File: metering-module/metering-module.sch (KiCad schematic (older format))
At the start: 36 parts, among them J1 North, J2 South, J3 West, J4 East, Q1 MMBT3904, Q2 MMBT3904, U1 LTV-817S, U2 LTV-817S, U3 BA033CC0FP-E2, U4 MAX3486, U5 MAX3486, U6 MCP23008-xSO

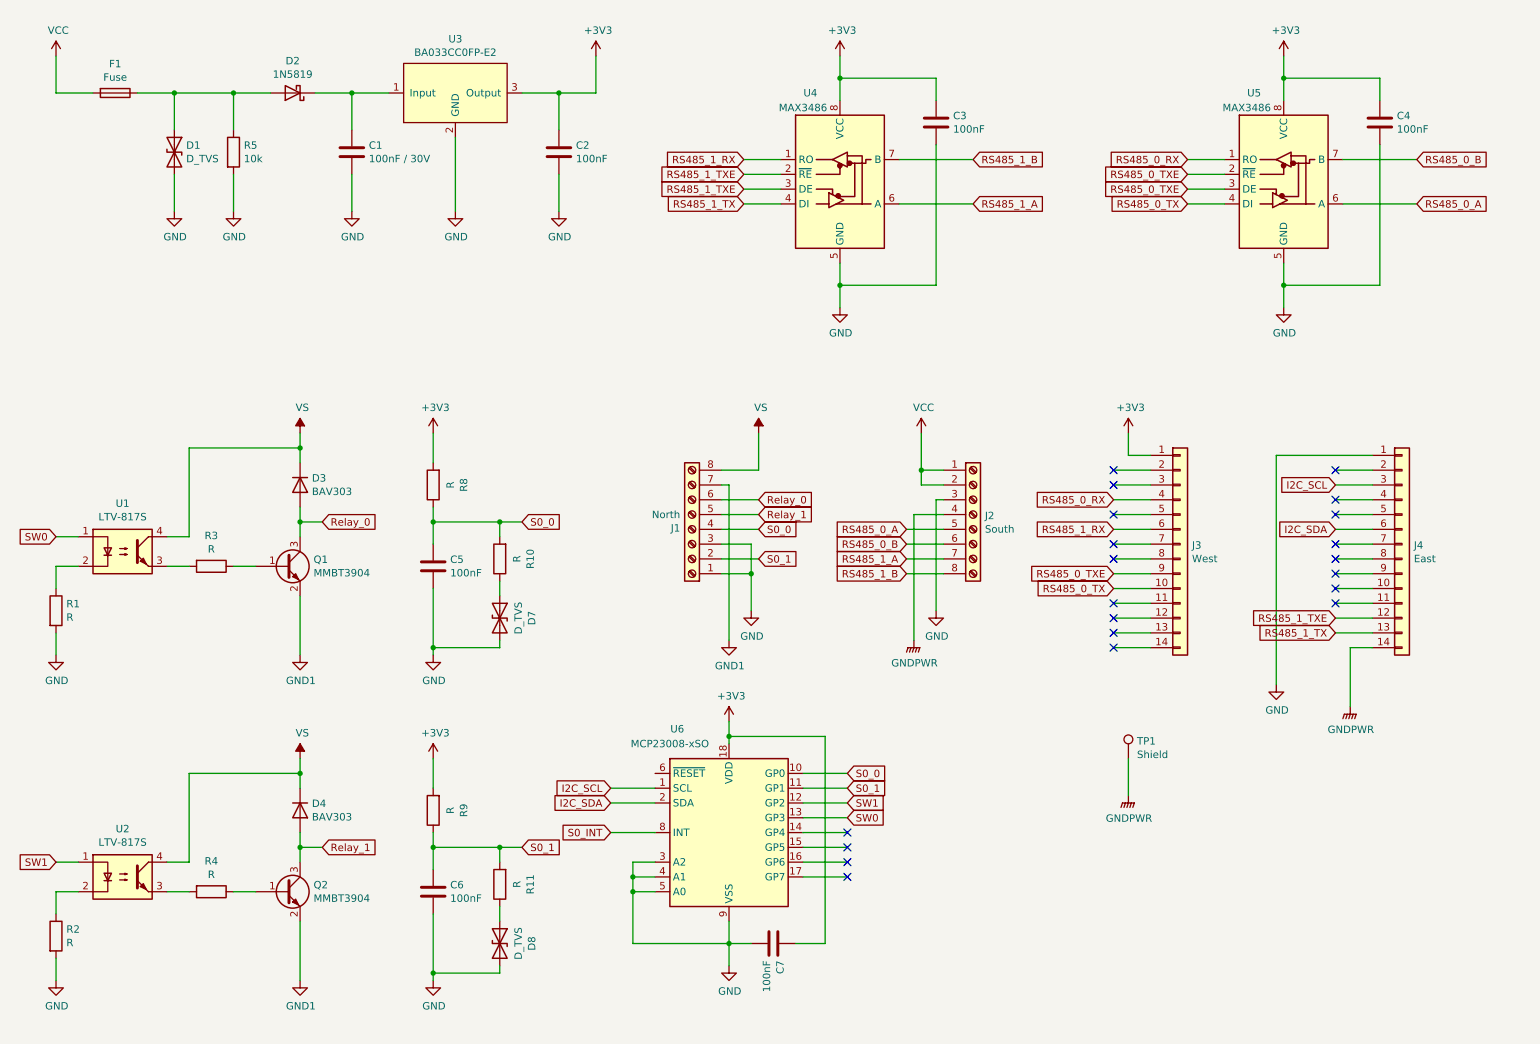
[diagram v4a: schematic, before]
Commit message: Introduce new serial numbering scheme
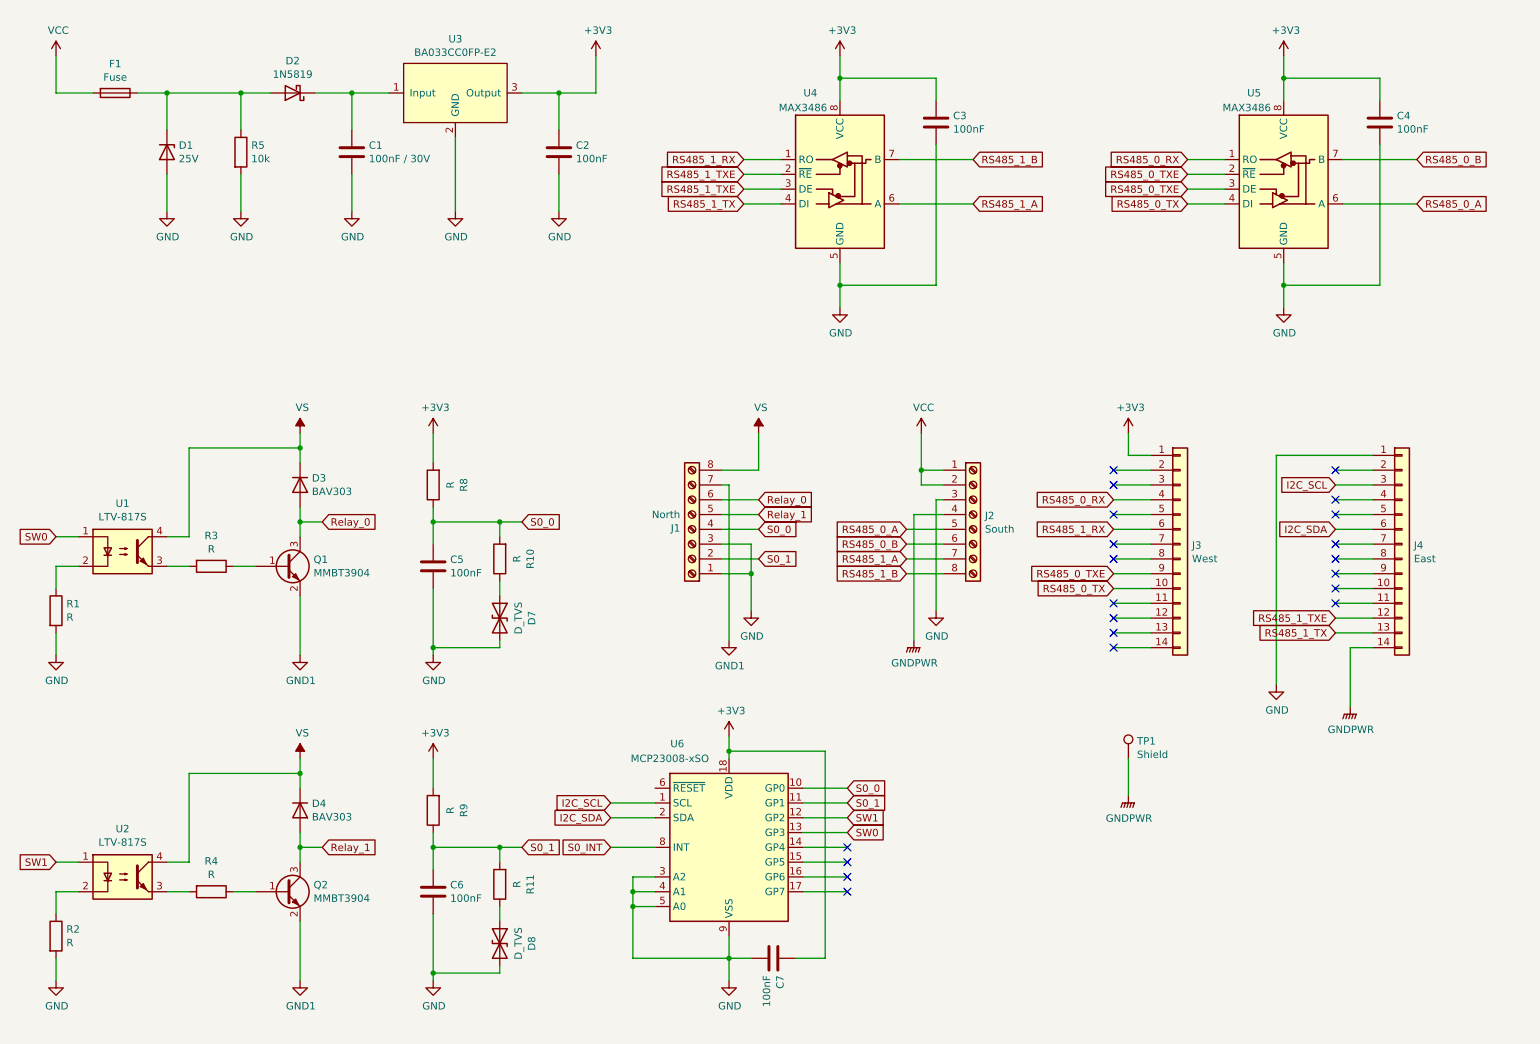
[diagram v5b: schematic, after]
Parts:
- removed D1: D_TVS, Diode_SMD:D_SOD-323_HandSoldering, symbol Device:D_TVS
- added D1: 25V, Diode_SMD:D_SOD-523, symbol Device:D_Zener
- C1: Price (none) -> 0.24; Product (none) -> https://www.mouser.de/ProductDetail/KEMET/C1206C104M6RACTU?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
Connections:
- net GND: now also D1.2 (A)
- net at D2.2 (A), F1.1, R5.1: now also D1.1 (K)
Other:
- moved on the sheet: C7, R5, U6
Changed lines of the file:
@@
-$EndComp
-$Comp
-L Device:D_TVS D1
-U 1 1 61930B40
-P 1950 1750
-F 0 "D1" V 1904 1830 50  0000 L CNN
-F 1 "D_TVS" V 1995 1830 50  0000 L CNN
-F 2 "Diode_SMD:D_SOD-323_HandSoldering" H 1950 1750 50  0001 C CNN
-F 3 "~" H 1950 1750 50  0001 C CNN
-	1    1950 1750
-	0    1    1    0
 $EndComp
 $Comp
@@
 L Device:R R5
 U 1 1 61931725
-P 2350 1750
-F 0 "R5" H 2420 1796 50  0000 L CNN
-F 1 "10k" H 2420 1705 50  0000 L CNN
-F 2 "Resistor_SMD:R_1206_3216Metric_Pad1.30x1.75mm_HandSolder" V 2280 1750 50  0001 C CNN
-F 3 "~" H 2350 1750 50  0001 C CNN
-	1    2350 1750
+P 2400 1750
+F 0 "R5" H 2470 1796 50  0000 L CNN
+F 1 "10k" H 2470 1705 50  0000 L CNN
+F 2 "Resistor_SMD:R_1206_3216Metric_Pad1.30x1.75mm_HandSolder" V 2330 1750 50  0001 C CNN
+F 3 "~" H 2400 1750 50  0001 C CNN
+	1    2400 1750
 	1    0    0    -1
 $EndComp
@@
 F 1 "100nF / 30V" H 3265 1705 50  0000 L CNN
 F 2 "Capacitor_SMD:C_1206_3216Metric_Pad1.33x1.80mm_HandSolder" H 3188 1600 50  0001 C CNN
-F 3 "~" H 3150 1750 50  0001 C CNN
+F 3 "https://www.mouser.de/datasheet/2/212/KEM_C1002_X7R_SMD-1102033.pdf" H 3150 1750 50  0001 C CNN
+F 4 "https://www.mouser.de/ProductDetail/KEMET/C1206C104M6RACTU?qs=F5EMLAvA7IBTviv6fCZN3A%3D%3D" H 3150 1750 50  0001 C CNN "Product"
+F 5 "0.24" H 3150 1750 50  0001 C CNN "Price"
 	1    3150 1750
 	1    0    0    -1
@@
 	3150 1350 3400 1350
 Wire Wire Line
-	2350 1600 2350 1350
-Wire Wire Line
-	1700 1350 1950 1350
-Connection ~ 2350 1350
-Wire Wire Line
-	2350 1350 2600 1350
-Wire Wire Line
-	1950 1600 1950 1350
-Connection ~ 1950 1350
-Wire Wire Line
-	1950 1350 2350 1350
+	2400 1600 2400 1350
+Wire Wire Line
+	1700 1350 1900 1350
+Wire Wire Line
+	1900 1600 1900 1350
 Wire Wire Line
 	4300 1350 4550 1350
@@
 L power:GND #PWR0106
 U 1 1 6193D7EC
-P 2350 2150
-F 0 "#PWR0106" H 2350 1900 50  0001 C CNN
-F 1 "GND" H 2355 1977 50  0000 C CNN
-F 2 "" H 2350 2150 50  0001 C CNN
-F 3 "" H 2350 2150 50  0001 C CNN
-	1    2350 2150
+P 2400 2150
+F 0 "#PWR0106" H 2400 1900 50  0001 C CNN
+F 1 "GND" H 2405 1977 50  0000 C CNN
+F 2 "" H 2400 2150 50  0001 C CNN
+F 3 "" H 2400 2150 50  0001 C CNN
+	1    2400 2150
 	1    0    0    -1
 $EndComp
@@
 L power:GND #PWR0107
 U 1 1 6193DD3C
-P 1950 2150
-F 0 "#PWR0107" H 1950 1900 50  0001 C CNN
-F 1 "GND" H 1955 1977 50  0000 C CNN
-F 2 "" H 1950 2150 50  0001 C CNN
-F 3 "" H 1950 2150 50  0001 C CNN
-	1    1950 2150
-	1    0    0    -1
-$EndComp
-Wire Wire Line
-	1950 1900 1950 2150
-Wire Wire Line
-	2350 2150 2350 1900
+P 1900 2150
+F 0 "#PWR0107" H 1900 1900 50  0001 C CNN
+F 1 "GND" H 1905 1977 50  0000 C CNN
+F 2 "" H 1900 2150 50  0001 C CNN
+F 3 "" H 1900 2150 50  0001 C CNN
+	1    1900 2150
+	1    0    0    -1
+$EndComp
+Wire Wire Line
+	1900 1900 1900 2150
+Wire Wire Line
+	2400 2150 2400 1900
 Wire Wire Line
 	3150 1900 3150 2150
@@
 Wire Wire Line
 	7000 3650 7000 3900
-Text GLabel 6500 5950 2    50   Input ~ 0
+Text GLabel 6500 6050 2    50   Input ~ 0
 S0_0
-Text GLabel 6500 6050 2    50   Input ~ 0
+Text GLabel 6500 6150 2    50   Input ~ 0
 S0_1
+Text GLabel 6500 6350 2    50   Input ~ 0
+SW0
 Text GLabel 6500 6250 2    50   Input ~ 0
-SW0
-Text GLabel 6500 6150 2    50   Input ~ 0
 SW1
 Wire Wire Line
@@
 L Interface_Expansion:MCP23008-xSO U6
 U 1 1 61EB4389
-P 5700 6350
-F 0 "U6" H 5350 7050 50  0000 C CNN
-F 1 "MCP23008-xSO" H 5300 6950 50  0000 C CNN
-F 2 "Package_SO:SOIC-18W_7.5x11.6mm_P1.27mm" H 5700 5300 50  0001 C CNN
-F 3 "http://ww1.microchip.com/downloads/en/DeviceDoc/MCP23008-MCP23S08-Data-Sheet-20001919F.pdf" H 7000 5150 50  0001 C CNN
-	1    5700 6350
+P 5700 6450
+F 0 "U6" H 5350 7150 50  0000 C CNN
+F 1 "MCP23008-xSO" H 5300 7050 50  0000 C CNN
+F 2 "Package_SO:SOIC-18W_7.5x11.6mm_P1.27mm" H 5700 5400 50  0001 C CNN
+F 3 "http://ww1.microchip.com/downloads/en/DeviceDoc/MCP23008-MCP23S08-Data-Sheet-20001919F.pdf" H 7000 5250 50  0001 C CNN
+	1    5700 6450
 	1    0    0    -1
 $EndComp
@@
 L Device:C C7
 U 1 1 61F32AD8
-P 6000 7100
-F 0 "C7" H 6115 7146 50  0000 L CNN
-F 1 "100nF" H 6115 7055 50  0000 L CNN
-F 2 "Capacitor_SMD:C_1206_3216Metric_Pad1.33x1.80mm_HandSolder" H 6038 6950 50  0001 C CNN
-F 3 "~" H 6000 7100 50  0001 C CNN
-	1    6000 7100
+P 6000 7200
+F 0 "C7" H 6115 7246 50  0000 L CNN
+F 1 "100nF" H 6115 7155 50  0000 L CNN
+F 2 "Capacitor_SMD:C_1206_3216Metric_Pad1.33x1.80mm_HandSolder" H 6038 7050 50  0001 C CNN
+F 3 "~" H 6000 7200 50  0001 C CNN
+	1    6000 7200
 	0    1    1    0
 $EndComp
@@
 L power:+3V3 #PWR0127
 U 1 1 61F36D22
-P 5700 5600
-F 0 "#PWR0127" H 5700 5450 50  0001 C CNN
-F 1 "+3V3" H 5715 5773 50  0000 C CNN
-F 2 "" H 5700 5600 50  0001 C CNN
-F 3 "" H 5700 5600 50  0001 C CNN
-	1    5700 5600
+P 5700 5700
+F 0 "#PWR0127" H 5700 5550 50  0001 C CNN
+F 1 "+3V3" H 5715 5873 50  0000 C CNN
+F 2 "" H 5700 5700 50  0001 C CNN
+F 3 "" H 5700 5700 50  0001 C CNN
+	1    5700 5700
 	1    0    0    -1
 $EndComp
@@
 L power:GND #PWR0133
 U 1 1 61F37FD9
-P 5700 7250
-F 0 "#PWR0133" H 5700 7000 50  0001 C CNN
-F 1 "GND" H 5705 7077 50  0000 C CNN
-F 2 "" H 5700 7250 50  0001 C CNN
-F 3 "" H 5700 7250 50  0001 C CNN
-	1    5700 7250
-	1    0    0    -1
-$EndComp
-Wire Wire Line
-	5700 5600 5700 5700
-Wire Wire Line
-	5700 6950 5700 7100
-Wire Wire Line
-	5850 7100 5700 7100
-Connection ~ 5700 7100
-Wire Wire Line
-	5700 7100 5700 7250
-Wire Wire Line
-	6150 7100 6350 7100
-Wire Wire Line
-	6350 7100 6350 5700
-Wire Wire Line
-	6350 5700 5700 5700
-Connection ~ 5700 5700
-Wire Wire Line
-	5700 5700 5700 5750
+P 5700 7350
+F 0 "#PWR0133" H 5700 7100 50  0001 C CNN
+F 1 "GND" H 5705 7177 50  0000 C CNN
+F 2 "" H 5700 7350 50  0001 C CNN
+F 3 "" H 5700 7350 50  0001 C CNN
+	1    5700 7350
+	1    0    0    -1
+$EndComp
+Wire Wire Line
+	5700 5700 5700 5800
+Wire Wire Line
+	5700 7050 5700 7200
+Wire Wire Line
+	5850 7200 5700 7200
+Connection ~ 5700 7200
+Wire Wire Line
+	5700 7200 5700 7350
+Wire Wire Line
+	6150 7200 6350 7200
+Wire Wire Line
+	6350 7200 6350 5800
+Wire Wire Line
+	6350 5800 5700 5800
+Connection ~ 5700 5800
+Wire Wire Line
+	5700 5800 5700 5850
 NoConn ~ 9800 4700
 NoConn ~ 8300 4900
@@
 NoConn ~ 8300 4200
 Wire Wire Line
-	6200 5950 6500 5950
-Wire Wire Line
 	6200 6050 6500 6050
 Wire Wire Line
-	6500 6150 6200 6150
-Wire Wire Line
-	6200 6250 6500 6250
-NoConn ~ 6500 6350
+	6200 6150 6500 6150
+Wire Wire Line
+	6500 6250 6200 6250
+Wire Wire Line
+	6200 6350 6500 6350
 NoConn ~ 6500 6450
 NoConn ~ 6500 6550
 NoConn ~ 6500 6650
-Wire Wire Line
-	6500 6350 6200 6350
+NoConn ~ 6500 6750
 Wire Wire Line
 	6500 6450 6200 6450
@@
 Wire Wire Line
 	6500 6650 6200 6650
+Wire Wire Line
+	6500 6750 6200 6750
+Text GLabel 4900 6250 0    50   Input ~ 0
+I2C_SDA
 Text GLabel 4900 6150 0    50   Input ~ 0
-I2C_SDA
-Text GLabel 4900 6050 0    50   Input ~ 0
 I2C_SCL
 Text GLabel 9800 4300 0    50   Input ~ 0
@@
 	9800 4800 10050 4800
 Wire Wire Line
-	4900 6050 5200 6050
-Wire Wire Line
 	4900 6150 5200 6150
-Text GLabel 4900 6350 0    50   Input ~ 0
+Wire Wire Line
+	4900 6250 5200 6250
+Text GLabel 4900 6450 0    50   Input ~ 0
 S0_INT
 Wire Wire Line
-	4900 6350 5200 6350
-Wire Wire Line
-	5200 6550 5050 6550
-Wire Wire Line
-	5050 6550 5050 6650
-Wire Wire Line
-	5050 7100 5700 7100
-Wire Wire Line
-	5050 6650 5200 6650
-Connection ~ 5050 6650
+	4900 6450 5200 6450
+Wire Wire Line
+	5200 6650 5050 6650
 Wire Wire Line
 	5050 6650 5050 6750
 Wire Wire Line
-	5200 6750 5050 6750
+	5050 7200 5700 7200
+Wire Wire Line
+	5050 6750 5200 6750
 Connection ~ 5050 6750
 Wire Wire Line
-	5050 6750 5050 7100
+	5050 6750 5050 6850
+Wire Wire Line
+	5200 6850 5050 6850
+Connection ~ 5050 6850
+Wire Wire Line
+	5050 6850 5050 7200
+$Comp
+L Device:D_Zener D1
+U 1 1 62076EFE
+P 1900 1750
+F 0 "D1" V 1854 1830 50  0000 L CNN
+F 1 "25V" V 1945 1830 50  0000 L CNN
+F 2 "Diode_SMD:D_SOD-523" H 1900 1750 50  0001 C CNN
+F 3 "https://www.mouser.de/datasheet/2/80/CPDU_Series_HF__RevF396351-2505940.pdf" H 1900 1750 50  0001 C CNN
+F 4 "https://www.mouser.de/ProductDetail/Comchip-Technology/CPDU24V?qs=tw%252BuQ%2FB6PO0bamw1irr2%252Bg%3D%3D" V 1900 1750 50  0001 C CNN "Product"
+F 5 "0.40" V 1900 1750 50  0001 C CNN "Price"
+	1    1900 1750
+	0    1    1    0
+$EndComp
+Connection ~ 1900 1350
+Connection ~ 2400 1350
+Wire Wire Line
+	2400 1350 2600 1350
+Wire Wire Line
+	1900 1350 2400 1350
 $EndSCHEMATC

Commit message: Work on Ethernet module
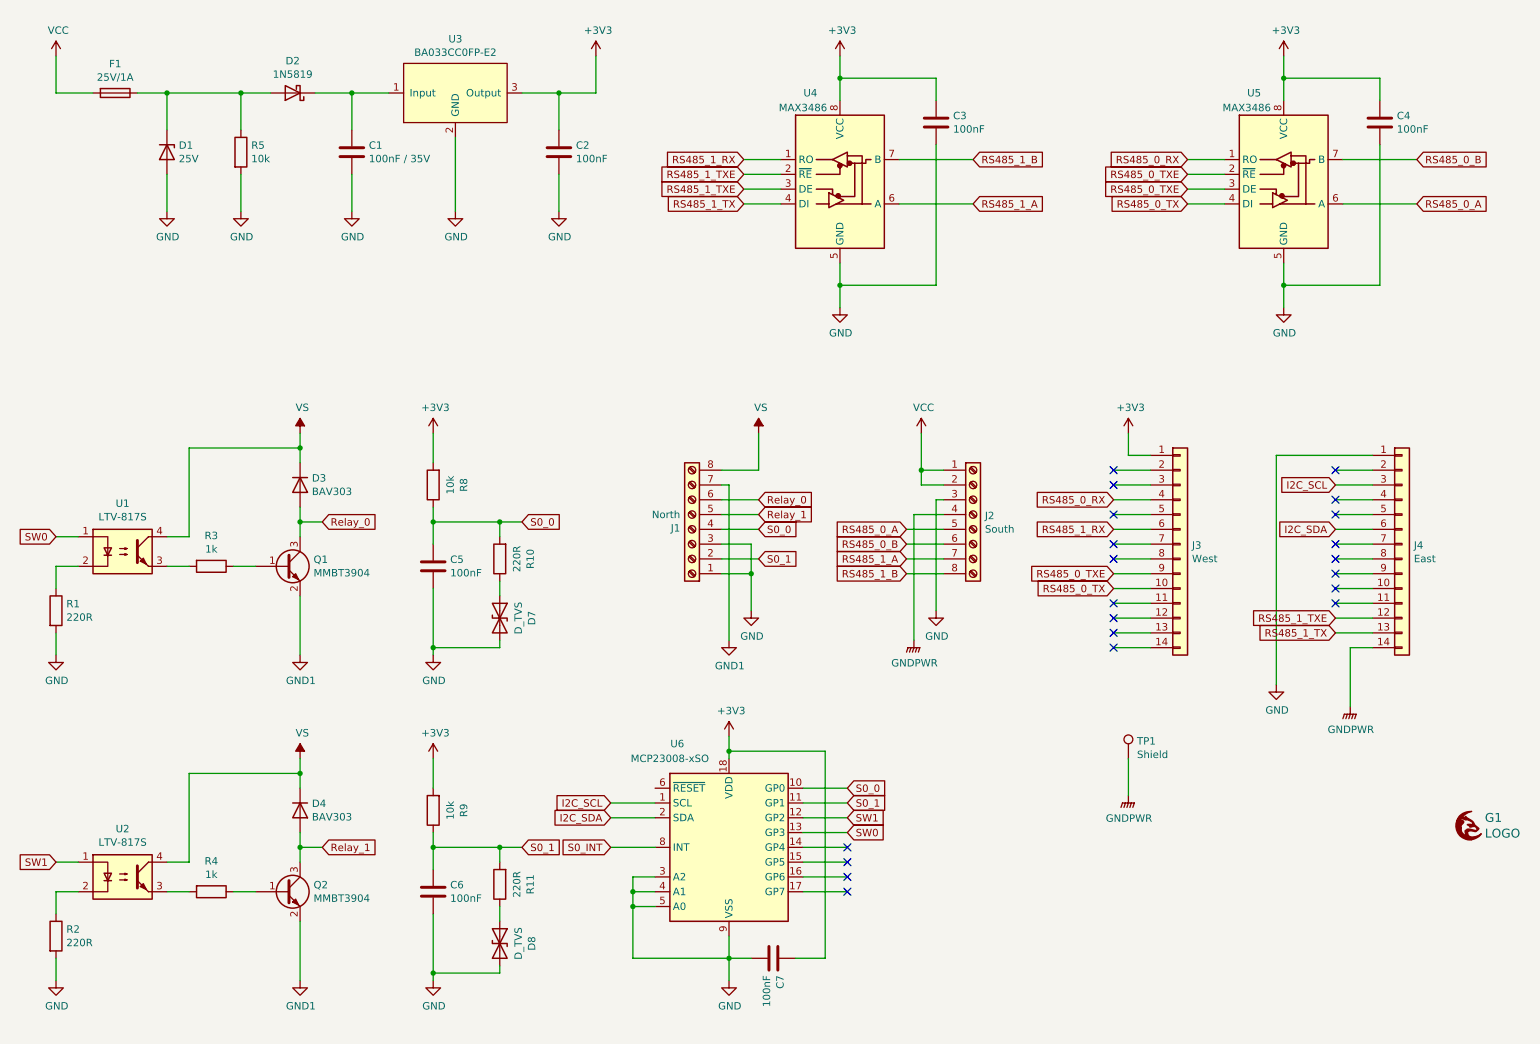
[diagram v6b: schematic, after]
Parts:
- added G1: LOGO, images:grayc-logo-negative, symbol grayc-logo-negative:LOGO
- C1: value 100nF / 30V -> 100nF / 35V
- C2, C3, C4, C5, C6, C7: Price (none) -> 0.24; Product (none) -> https://www.mouser.de/ProductDetail/KEMET/C1206C104M6RACTU?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
- D2: Price (none) -> 0.25; Product (none) -> https://www.mouser.de/ProductDetail/Diodes-Incorporated/1N5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
- D3, D4: Price (none) -> 0.20; Product (none) -> https://www.mouser.de/ProductDetail/Vishay-Semiconductors/B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
- D7, D8: Price (none) -> 0.32; Product (none) -> https://www.mouser.de/ProductDetail/Bourns/CG0603MLC-33LE?q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
- F1: value Fuse -> 25V/1A; Price (none) -> 0.93; Product (none) -> https://www.mouser.de/ProductDetail/Bourns/SF-1206HIA100M-2
- J1, J2: Price (none) -> 4.85; Product (none) -> https://www.mouser.de/ProductDetail/Phoenix-Contact/1727078
- J3, J4: Price (none) -> 0.45; Product (none) -> https://www.mouser.de/ProductDetail/Harwin/M20-9991446
- Q1, Q2: Price (none) -> 0.09; Product (none) -> https://www.mouser.de/ProductDetail/Nexperia/MMBT3904215
- R1, R10, R11, R2: value R -> 220R; Price (none) -> 0.08; Product (none) -> https://www.mouser.de/ProductDetail/TE-Connectivity-Holswor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
- R3, R4: value R -> 1k; Price (none) -> 0.10; Product (none) -> https://www.mouser.de/ProductDetail/KOA-Speer/RK73B2BTTDD10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
- R5: Price (none) -> 0.08; Product (none) -> https://www.mouser.de/ProductDetail/Bourns/CR1206-JW-103ELF
- R8, R9: value R -> 10k; Price (none) -> 0.08; Product (none) -> https://www.mouser.de/ProductDetail/Bourns/CR1206-JW-103ELF
- U1, U2: Price (none) -> 0.40; Product (none) -> https://www.mouser.de/ProductDetail/Lite-On/LTV-817S
- U3: Price (none) -> 0.97; Product (none) -> https://www.mouser.de/ProductDetail/ROHM-Semiconductor/BA03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
- U4, U5: Price (none) -> 3.71; Product (none) -> https://www.mouser.de/ProductDetail/Maxim-Integrated/MAX348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
- U6: Price (none) -> 1.10; Product (none) -> https://www.mouser.de/ProductDetail/Microchip-Technology/MC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
